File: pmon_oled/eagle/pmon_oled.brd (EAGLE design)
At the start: 60 x 60 mm, 36 parts, among them J1 USB, J2 USB, J4 PINHD-1X3, J5 PINHD-2X3, Q1 16Mhz, U1 LTC2943, U2 FT232RL, U3 LT1764AEQ, U4 ATMEGA328TQFP32

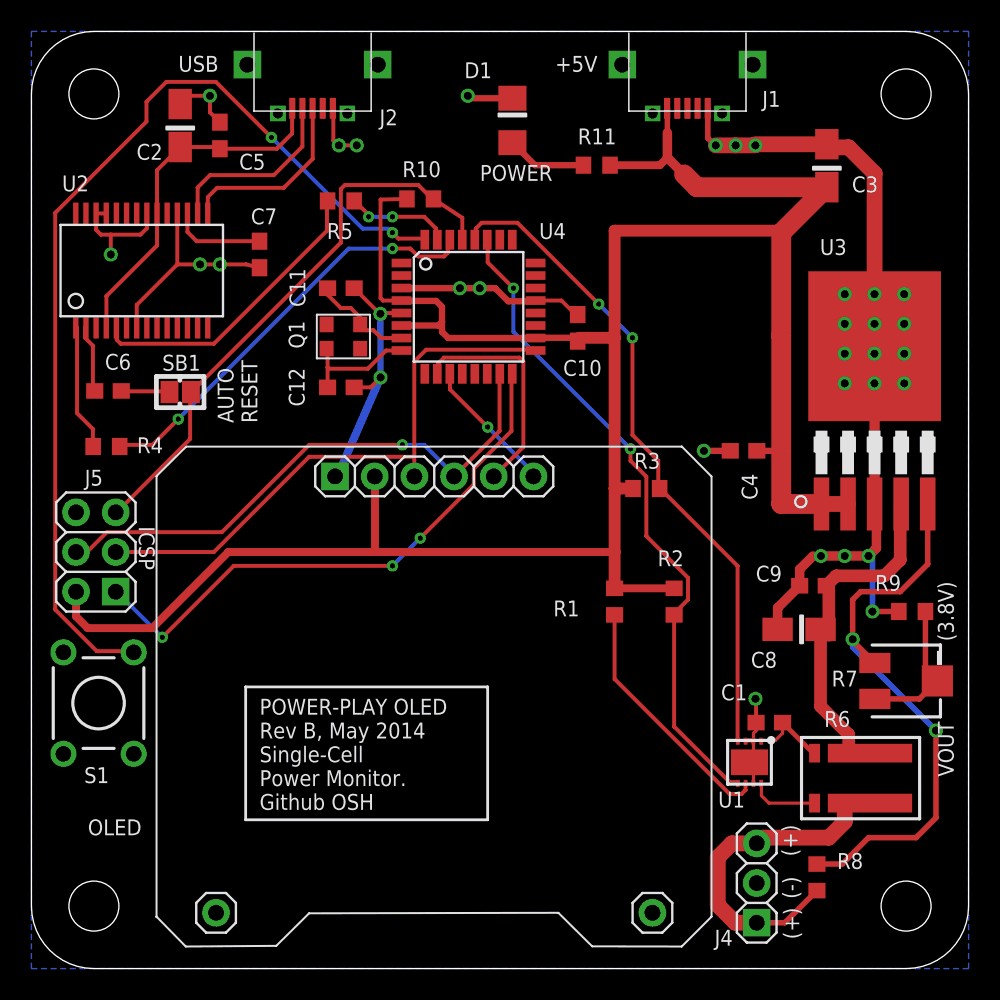
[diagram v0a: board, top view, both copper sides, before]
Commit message: Removed power led, added vias to the solder jumpers.
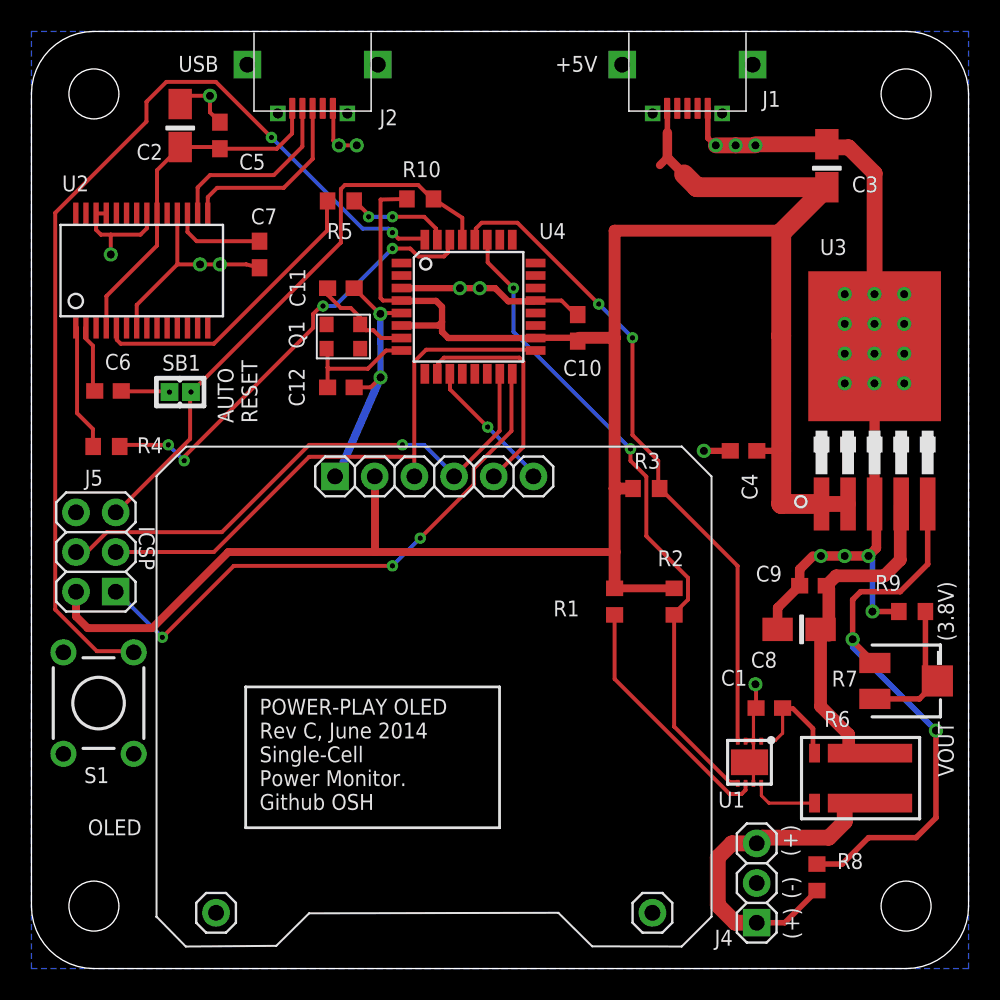
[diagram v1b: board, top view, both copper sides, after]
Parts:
- removed D1: BLUE, pmon_oled:1206-LED
- removed R11: 3K3, pmon_oled:R0603
- moved C1 0.93 mm to (47.2, 16.7)
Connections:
- removed net N$17: D1.A, R11.2
- net +5V: no longer R11.1
- net GND: no longer D1.C
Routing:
- net N$17: track 5.15 -> 0.00 mm
- net +5V: track 159.4 -> 156.1 mm
- net SENSE+: track 5.11 -> 7.34 mm
- net GND: track 123.4 -> 121.6 mm, vias 32 -> 31
- net SER_RX: track 27.5 -> 29.0 mm, vias 2 -> 4
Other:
- board text added: "POWER-PLAY OLED - REV C OSH GITHUB"
- board text added: "POWER-PLAY OLED Rev C, June 2014 Single-Cell Power Monitor. Github OSH"
- board text removed: "POWER"
- board text removed: "POWER-PLAY OLED - REV B OSH GITHUB"
- board text removed: "POWER-PLAY OLED Rev B, May 2014 Single-Cell Power Monitor. Github OSH"

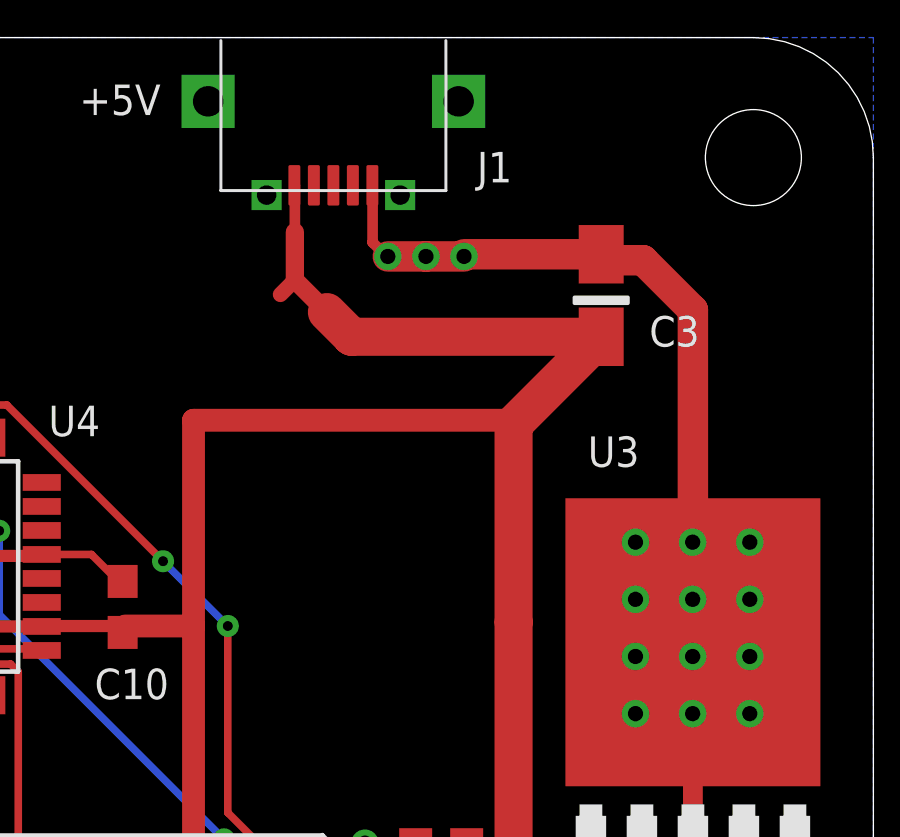
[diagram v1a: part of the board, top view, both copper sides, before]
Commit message: Added pmon_5v BOM. Minor tweaks of schematics and layouts.
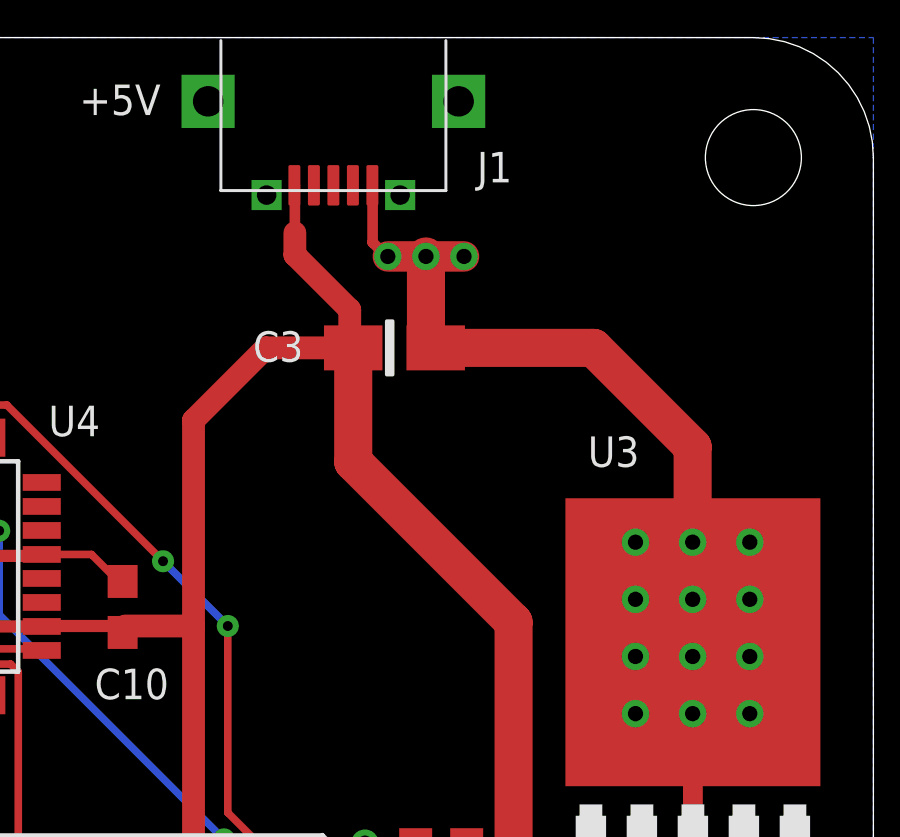
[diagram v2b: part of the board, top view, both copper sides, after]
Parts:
- moved C3 7.11 mm to (44.0, 49.7), turned to 180 degrees
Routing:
- net +5V: track 156.1 -> 143.7 mm
- net GND: track 121.6 -> 120.4 mm
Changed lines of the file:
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@@
 <attribute name="NAME" x="46.064521875" y="19.257865625" size="1.016" layer="25" font="vector" ratio="10"/>
 </element>
-<element name="C3" library="pmon_oled" package="A/3216-18R" value="10uF" x="50.927" y="51.402" smashed="yes" rot="R270">
-<attribute name="NAME" x="52.531409375" y="49.70061875" size="1.016" layer="25" font="vector" ratio="10"/>
+<element name="C3" library="pmon_oled" package="A/3216-18R" value="10uF" x="44.036" y="49.657" smashed="yes" rot="R180">
+<attribute name="NAME" x="39.323409375" y="49.19261875" size="1.016" layer="25" font="vector" ratio="10"/>
 </element>
 <element name="C4" library="pmon_oled" package="C0603" value="0.1uF" x="45.593" y="33.147" smashed="yes" rot="R180">
@@
 <wire x1="43.3" y1="55.075" x2="43.307" y2="55.075" width="0.3556" layer="1"/>
 <wire x1="43.307" y1="55.075" x2="43.307" y2="53.174" width="0.3556" layer="1"/>
-<wire x1="50.927" y1="52.777" x2="50.927" y2="52.705" width="0.3556" layer="1"/>
 <wire x1="53.984" y1="29.745" x2="54.102" y2="29.627" width="0.3556" layer="1"/>
 <wire x1="54.102" y1="29.627" x2="54.102" y2="26.924" width="0.6096" layer="1"/>
@@
 <via x="52.07" y="26.416" extent="1-16" drill="0.508"/>
 <via x="50.546" y="26.416" extent="1-16" drill="0.508"/>
-<wire x1="50.927" y1="52.705" x2="51.054" y2="52.578" width="0.762" layer="1"/>
-<wire x1="51.054" y1="52.578" x2="52.324" y2="52.578" width="1.016" layer="1"/>
-<wire x1="52.324" y1="52.578" x2="53.984" y2="50.918" width="1.016" layer="1"/>
-<wire x1="53.984" y1="50.918" x2="53.984" y2="39.845" width="1.016" layer="1"/>
 <via x="53.975" y="39.37" extent="1-16" drill="0.508"/>
 <via x="52.07" y="43.18" extent="1-16" drill="0.508"/>
@@
 <contactref element="S1" pad="A"/>
 <wire x1="45.085" y1="52.705" x2="46.355" y2="52.705" width="1.016" layer="1"/>
-<wire x1="50.927" y1="52.777" x2="46.355" y2="52.777" width="1.016" layer="1"/>
 <wire x1="46.355" y1="52.777" x2="46.355" y2="52.705" width="0.4064" layer="1"/>
 <wire x1="44.743" y1="33.147" x2="43.053" y2="33.147" width="0.4064" layer="1"/>
@@
 <wire x1="46.228" y1="16.637" x2="46.394" y2="16.637" width="0.4064" layer="1"/>
 <wire x1="46.394" y1="16.637" x2="46.394" y2="16.67965" width="0.4064" layer="1"/>
+<wire x1="45.411" y1="49.657" x2="50.673" y2="49.657" width="1.27" layer="1"/>
+<wire x1="50.673" y1="49.657" x2="53.975" y2="46.355" width="1.27" layer="1"/>
+<wire x1="53.975" y1="46.355" x2="53.975" y2="41.275" width="1.27" layer="1"/>
+<wire x1="45.085" y1="52.705" x2="45.085" y2="49.911" width="1.27" layer="1"/>
+<wire x1="45.085" y1="49.911" x2="45.466" y2="49.53" width="0.4064" layer="1"/>
 </signal>
 <signal name="+5V">
@@
 <contactref element="J1" pad="1"/>
 <wire x1="40.7" y1="55.075" x2="40.7162" y2="55.075" width="0.3556" layer="1"/>
-<wire x1="40.7162" y1="55.075" x2="40.7162" y2="53.5178" width="0.3556" layer="1"/>
-<wire x1="40.7162" y1="53.5178" x2="40.7162" y2="53.4924" width="0.3556" layer="1"/>
-<wire x1="40.7162" y1="53.5178" x2="40.7162" y2="51.9176" width="0.6096" layer="1"/>
-<wire x1="40.7162" y1="51.9176" x2="41.783" y2="50.8508" width="0.6096" layer="1"/>
+<wire x1="40.7162" y1="55.075" x2="40.7162" y2="53.4924" width="0.3556" layer="1"/>
 <wire x1="50.584" y1="29.745" x2="52.284" y2="29.745" width="1.016" layer="1"/>
 <wire x1="23.6944" y1="42.771" x2="23.7172" y2="42.7482" width="0.254" layer="1"/>
@@
 <wire x1="35.052" y1="40.386" x2="34.9758" y2="40.3098" width="0.254" layer="1"/>
 <wire x1="34.9758" y1="40.3098" x2="34.9758" y2="40.171" width="0.254" layer="1"/>
-<wire x1="40.7162" y1="51.9176" x2="40.2336" y2="51.435" width="0.508" layer="1"/>
 <wire x1="37.338" y1="24.345" x2="41.148" y2="24.345" width="0.508" layer="1"/>
 <wire x1="21.98" y1="31.51" x2="21.9964" y2="31.4936" width="0.508" layer="1"/>
@@
 <wire x1="48.006" y1="29.745" x2="48.006" y2="33.147" width="1.27" layer="1"/>
 <wire x1="48.006" y1="33.147" x2="48.006" y2="40.513" width="1.27" layer="1"/>
-<wire x1="48.006" y1="40.513" x2="48.006" y2="47.106" width="1.27" layer="1"/>
 <wire x1="46.443" y1="33.147" x2="48.006" y2="33.147" width="0.4064" layer="1"/>
 <wire x1="47.879" y1="36.957" x2="48.006" y2="36.957" width="0.4064" layer="1"/>
@@
 <wire x1="26.289" y1="40.767" x2="26.685" y2="40.371" width="0.4064" layer="1"/>
 <wire x1="26.685" y1="40.371" x2="32.2796" y2="40.371" width="0.4064" layer="1"/>
-<wire x1="50.927" y1="50.027" x2="42.6068" y2="50.027" width="1.27" layer="1"/>
-<wire x1="42.6068" y1="50.027" x2="41.783" y2="50.8508" width="1.27" layer="1"/>
-<wire x1="48.006" y1="47.106" x2="50.927" y2="50.027" width="1.27" layer="1"/>
 <wire x1="35.052" y1="40.386" x2="37.338" y2="40.386" width="0.762" layer="1"/>
 <wire x1="48.006" y1="40.386" x2="48.006" y2="40.513" width="0.762" layer="1"/>
@@
 <wire x1="38.52" y1="30.734" x2="37.338" y2="30.734" width="0.762" layer="1"/>
 <wire x1="37.338" y1="40.386" x2="37.338" y2="47.244" width="0.762" layer="1"/>
-<wire x1="37.338" y1="47.244" x2="48.006" y2="47.244" width="0.762" layer="1"/>
-<wire x1="48.006" y1="47.244" x2="48.006" y2="47.106" width="0.762" layer="1"/>
+<wire x1="42.661" y1="49.657" x2="42.661" y2="45.858" width="1.27" layer="1"/>
+<wire x1="42.661" y1="45.858" x2="48.006" y2="40.513" width="1.27" layer="1"/>
+<wire x1="37.338" y1="47.244" x2="39.751" y2="49.657" width="0.762" layer="1"/>
+<wire x1="39.751" y1="49.657" x2="42.661" y2="49.657" width="0.762" layer="1"/>
+<wire x1="42.661" y1="49.657" x2="42.545" y2="49.773" width="0.4064" layer="1"/>
+<wire x1="42.545" y1="49.773" x2="42.545" y2="50.927" width="0.762" layer="1"/>
+<wire x1="42.545" y1="50.927" x2="40.7162" y2="52.7558" width="0.762" layer="1"/>
+<wire x1="40.7162" y1="52.7558" x2="40.7162" y2="53.4924" width="0.762" layer="1"/>
 </signal>
 <signal name="RESET">

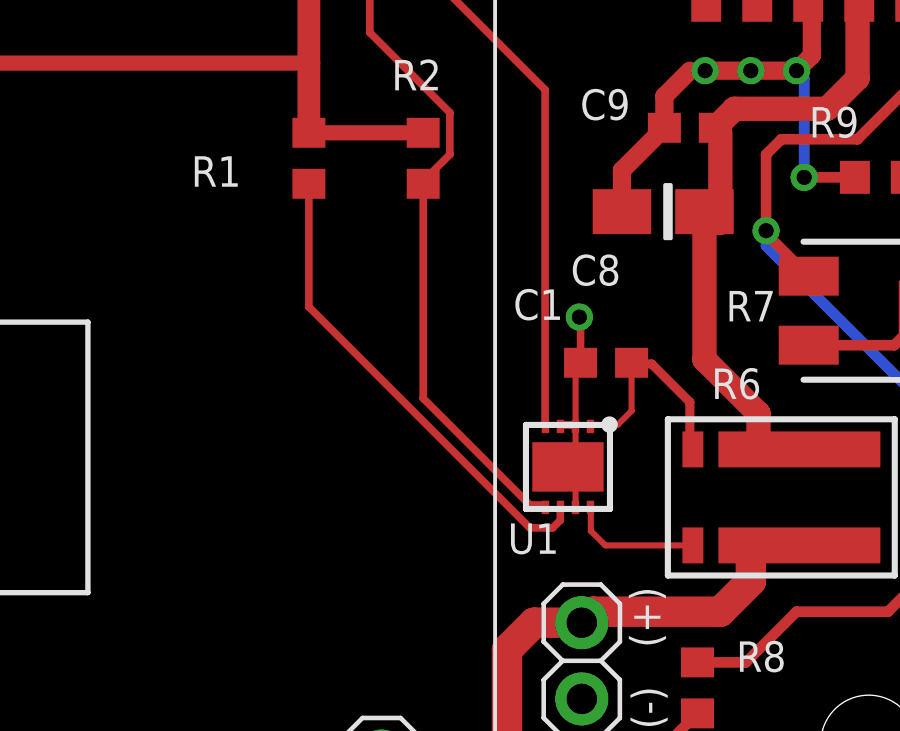
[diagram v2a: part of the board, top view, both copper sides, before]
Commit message: Updated the LTC2943 footpting to match the datasheet (longer pads now).
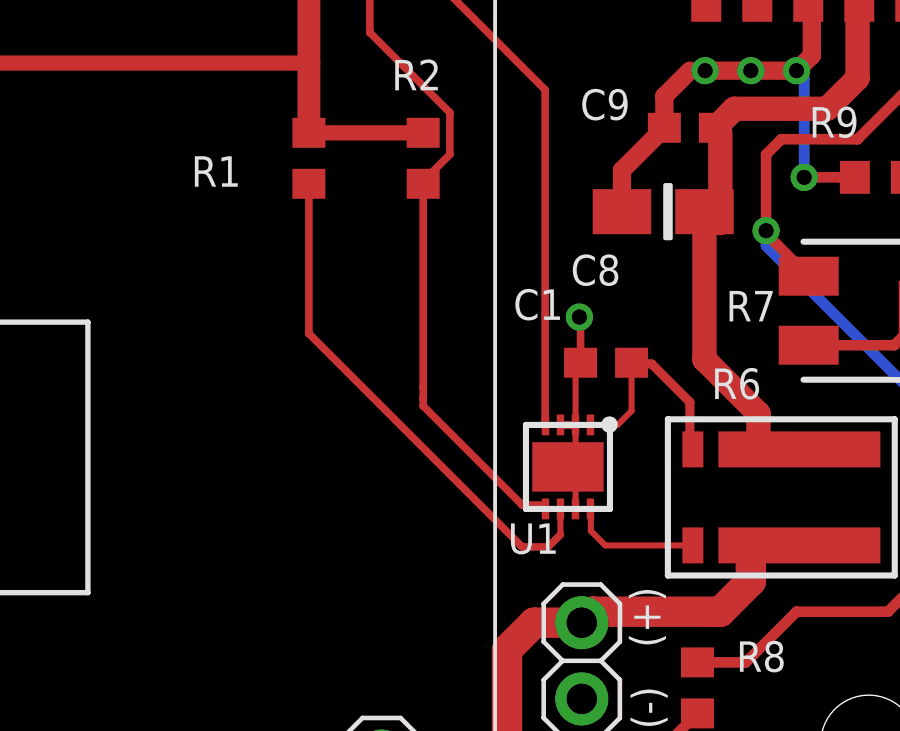
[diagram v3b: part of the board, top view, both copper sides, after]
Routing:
- net N$1: track 16.1 -> 17.4 mm
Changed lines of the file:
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@@
 <via x="28.702" y="43.561" extent="1-16" drill="0.508"/>
 <via x="27.432" y="43.561" extent="1-16" drill="0.508"/>
-<wire x1="46.224" y1="14.558" x2="46.228" y2="14.562" width="0.2032" layer="1"/>
+<wire x1="46.224" y1="14.608" x2="46.228" y2="14.562" width="0.2032" layer="1"/>
 <wire x1="46.228" y1="14.562" x2="46.228" y2="16.637" width="0.2032" layer="1"/>
 <wire x1="46.228" y1="16.637" x2="46.355" y2="16.637" width="0.2032" layer="1"/>
-<wire x1="46.224" y1="14.558" x2="46.228" y2="14.554" width="0.2032" layer="1"/>
+<wire x1="46.224" y1="14.608" x2="46.228" y2="14.554" width="0.2032" layer="1"/>
 <wire x1="46.228" y1="14.554" x2="46.228" y2="13.8176" width="0.2032" layer="1"/>
 <wire x1="46.228" y1="13.8176" x2="45.974" y2="13.5636" width="0.2032" layer="1"/>
 <wire x1="45.974" y1="13.5636" x2="45.974" y2="13.208" width="0.2032" layer="1"/>
-<wire x1="46.224" y1="11.858" x2="46.228" y2="11.862" width="0.2032" layer="1"/>
+<wire x1="46.224" y1="11.808" x2="46.228" y2="11.862" width="0.2032" layer="1"/>
 <wire x1="46.228" y1="11.862" x2="46.228" y2="12.5984" width="0.2032" layer="1"/>
 <wire x1="46.228" y1="12.5984" x2="45.974" y2="12.8524" width="0.2032" layer="1"/>
@@
 <wire x1="19.685" y1="52.705" x2="20.828" y2="52.705" width="0.254" layer="1"/>
 <wire x1="46.101" y1="14.605" x2="45.847" y2="14.605" width="0.254" layer="1"/>
-<wire x1="45.847" y1="14.605" x2="45.724" y2="14.558" width="0.254" layer="1"/>
-<wire x1="46.101" y1="14.605" x2="46.224" y2="14.558" width="0.254" layer="1"/>
+<wire x1="45.847" y1="14.605" x2="45.724" y2="14.608" width="0.254" layer="1"/>
+<wire x1="46.101" y1="14.605" x2="46.224" y2="14.608" width="0.254" layer="1"/>
 <wire x1="46.228" y1="16.637" x2="46.394" y2="16.637" width="0.4064" layer="1"/>
 <wire x1="46.394" y1="16.637" x2="46.394" y2="16.67965" width="0.4064" layer="1"/>
@@
 <contactref element="C1" pad="1"/>
 <contactref element="U1" pad="1"/>
-<wire x1="46.724" y1="14.558" x2="46.771" y2="14.605" width="0.2032" layer="1"/>
+<wire x1="46.724" y1="14.608" x2="46.771" y2="14.605" width="0.2032" layer="1"/>
 <wire x1="46.771" y1="14.605" x2="47.625" y2="14.605" width="0.2032" layer="1"/>
 <wire x1="47.625" y1="14.605" x2="48.094" y2="15.074" width="0.2032" layer="1"/>
@@
 <contactref element="R6" pad="V1"/>
 <contactref element="U1" pad="8"/>
-<wire x1="46.724" y1="11.858" x2="46.736" y2="11.846" width="0.2032" layer="1"/>
+<wire x1="46.724" y1="11.808" x2="46.736" y2="11.846" width="0.2032" layer="1"/>
 <wire x1="46.736" y1="11.846" x2="46.736" y2="11.0744" width="0.2032" layer="1"/>
 <wire x1="46.736" y1="11.0744" x2="47.2184" y2="10.592" width="0.2032" layer="1"/>
@@
 <wire x1="45.212" y1="25.781" x2="45.212" y2="14.605" width="0.254" layer="1"/>
 <wire x1="40.259" y1="30.734" x2="45.212" y2="25.781" width="0.254" layer="1"/>
-<wire x1="45.212" y1="14.605" x2="45.224" y2="14.558" width="0.254" layer="1"/>
+<wire x1="45.212" y1="14.605" x2="45.224" y2="14.608" width="0.254" layer="1"/>
 <wire x1="40.259" y1="30.734" x2="40.22" y2="30.734" width="0.254" layer="1"/>
 <wire x1="28.448" y1="47.371" x2="28.448" y2="46.736" width="0.254" layer="1"/>
@@
 <contactref element="U1" pad="5"/>
 <contactref element="U4" pad="27"/>
-<wire x1="44.704" y1="11.938" x2="45.212" y2="11.938" width="0.254" layer="1"/>
-<wire x1="41.148" y1="15.494" x2="44.704" y2="11.938" width="0.254" layer="1"/>
-<wire x1="41.148" y1="22.645" x2="41.148" y2="15.494" width="0.254" layer="1"/>
-<wire x1="45.212" y1="11.938" x2="45.224" y2="11.858" width="0.254" layer="1"/>
+<wire x1="44.45" y1="11.938" x2="45.212" y2="11.938" width="0.254" layer="1"/>
+<wire x1="41.148" y1="22.645" x2="41.148" y2="15.875" width="0.254" layer="1"/>
+<wire x1="41.148" y1="15.875" x2="41.148" y2="15.494" width="0.254" layer="1"/>
+<wire x1="45.212" y1="11.938" x2="45.224" y2="11.808" width="0.254" layer="1"/>
 <wire x1="29.21" y1="45.212" x2="29.21" y2="46.609" width="0.254" layer="1"/>
 <wire x1="30.861" y1="43.561" x2="29.21" y2="45.212" width="0.254" layer="1"/>
@@
 <via x="30.861" y="43.561" extent="1-16" drill="0.3302"/>
 <via x="38.354" y="33.274" extent="1-16" drill="0.3302"/>
+<wire x1="44.45" y1="11.938" x2="41.148" y2="15.24" width="0.254" layer="1"/>
+<wire x1="41.148" y1="15.24" x2="41.148" y2="15.494" width="0.254" layer="1"/>
 </signal>
 <signal name="N$18">
@@
 <contactref element="U1" pad="6"/>
 <contactref element="R1" pad="1"/>
-<wire x1="45.72" y1="11.43" x2="45.72" y2="11.811" width="0.254" layer="1"/>
-<wire x1="45.466" y1="11.176" x2="45.72" y2="11.43" width="0.254" layer="1"/>
-<wire x1="44.704" y1="11.176" x2="45.466" y2="11.176" width="0.254" layer="1"/>
-<wire x1="37.338" y1="18.542" x2="44.704" y2="11.176" width="0.254" layer="1"/>
-<wire x1="37.338" y1="22.645" x2="37.338" y2="18.542" width="0.254" layer="1"/>
-<wire x1="45.72" y1="11.811" x2="45.724" y2="11.858" width="0.254" layer="1"/>
+<wire x1="37.338" y1="22.645" x2="37.338" y2="17.653" width="0.254" layer="1"/>
+<wire x1="45.72" y1="11.811" x2="45.724" y2="11.808" width="0.254" layer="1"/>
+<wire x1="45.72" y1="11.811" x2="45.723440625" y2="11.811" width="0.254" layer="1"/>
+<wire x1="45.723440625" y1="11.811" x2="45.723440625" y2="10.950234375" width="0.2032" layer="1"/>
+<wire x1="45.723440625" y1="10.950234375" x2="45.31420625" y2="10.541" width="0.254" layer="1"/>
+<wire x1="45.31420625" y1="10.541" x2="44.45" y2="10.541" width="0.254" layer="1"/>
+<wire x1="44.45" y1="10.541" x2="37.338" y2="17.653" width="0.254" layer="1"/>
 </signal>
 <signal name="N$22">
